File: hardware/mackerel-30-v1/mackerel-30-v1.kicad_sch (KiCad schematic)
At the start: 0 parts

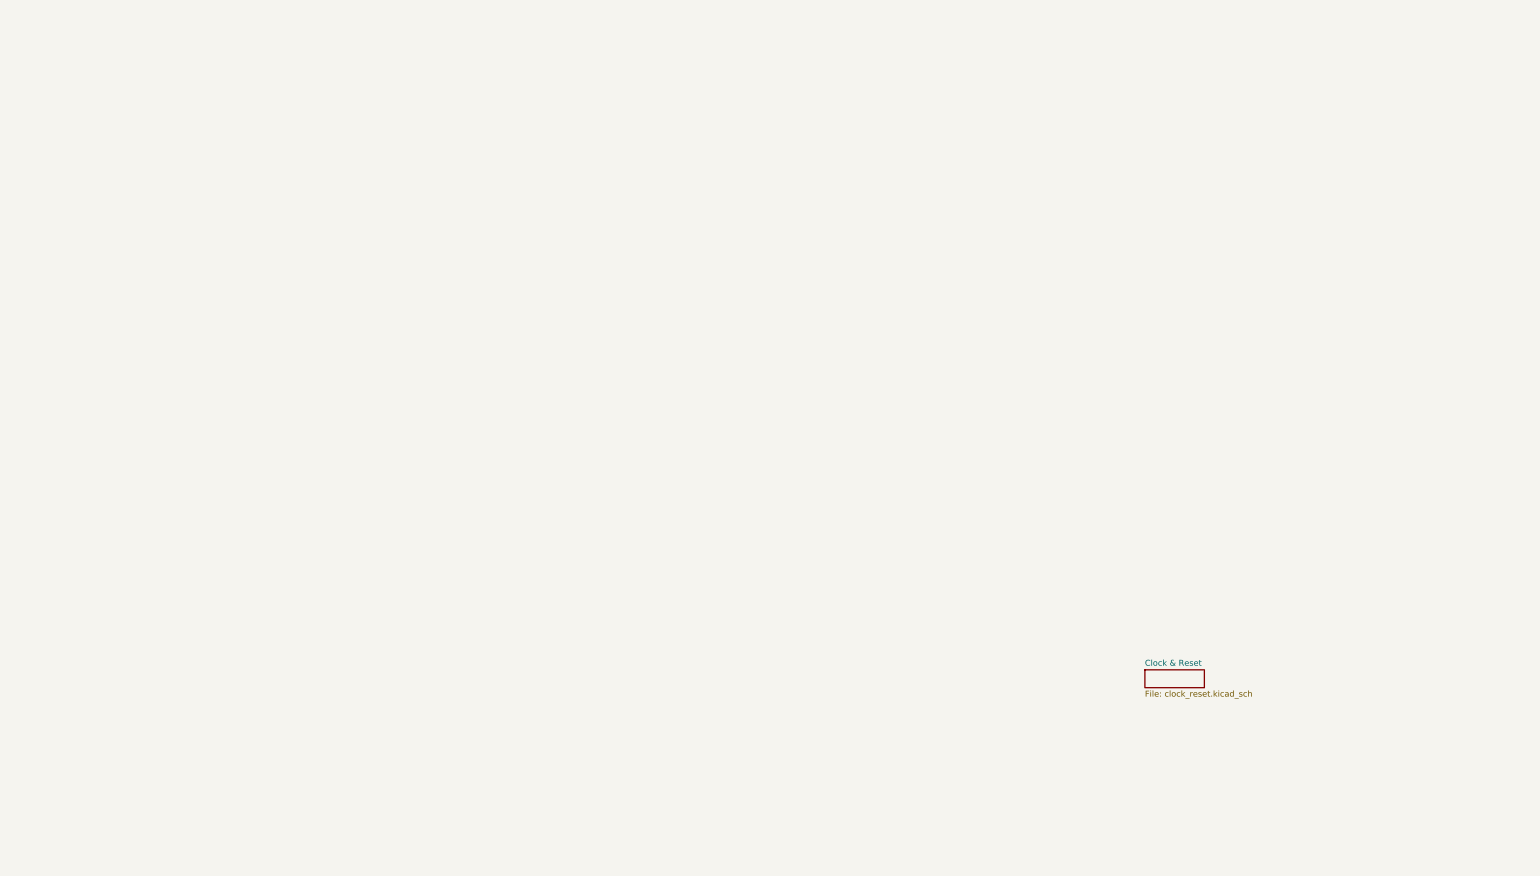
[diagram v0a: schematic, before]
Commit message: Mackerel-30: Label the 68030 pinout
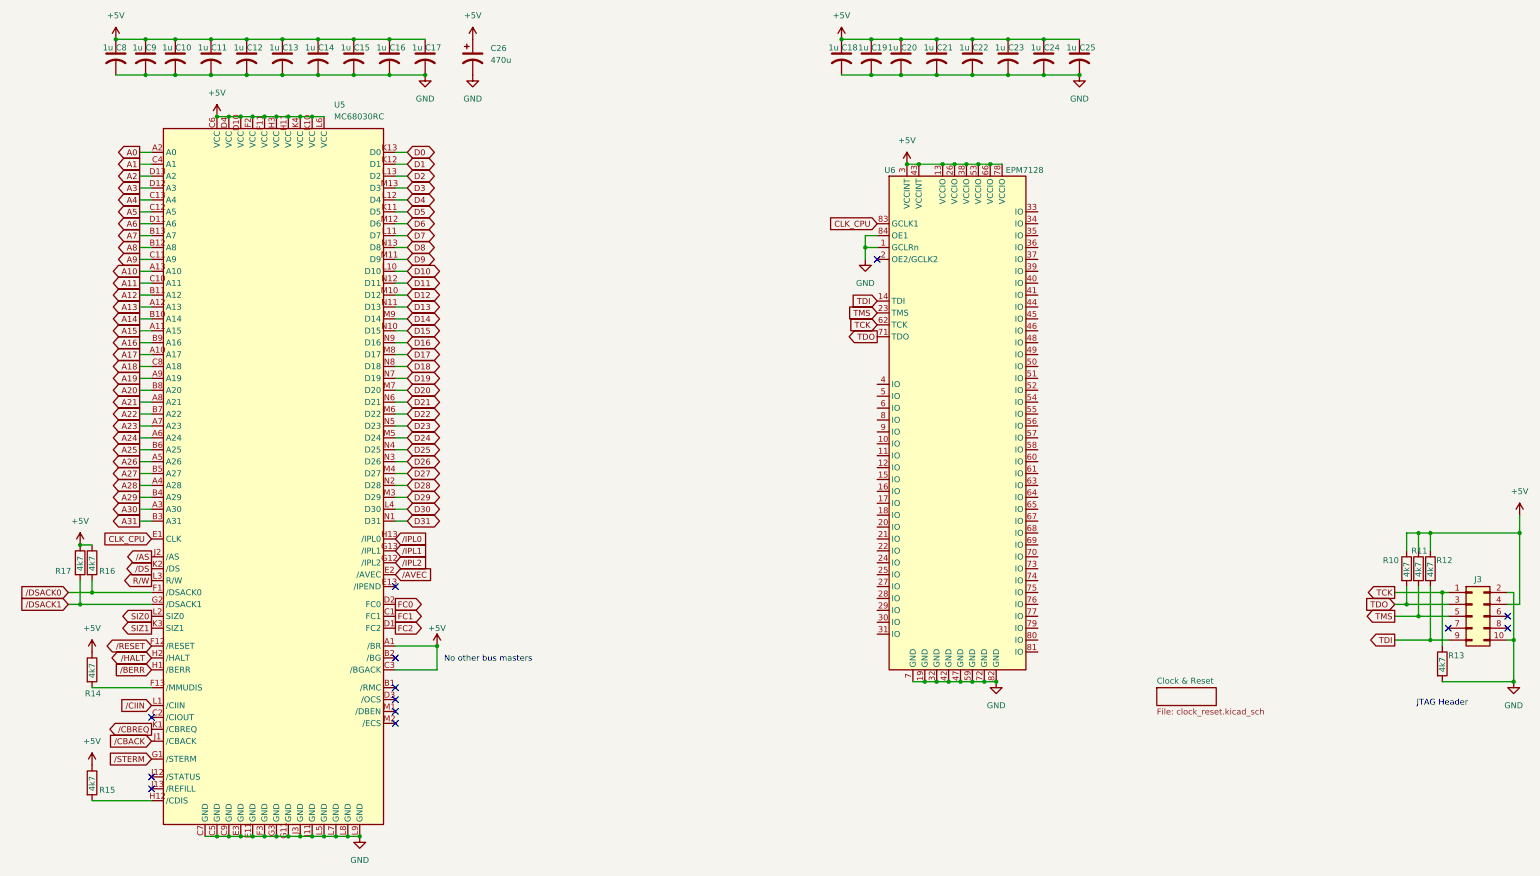
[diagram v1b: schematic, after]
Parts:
- added C10, C11, C12, C13, C14, C15, C16, C17, C18, C19, C20, C21, C22, C23, C24, C25, C8, C9: 1u, Capacitor_SMD:C_0805_2012Metric_Pad1.18x1.45mm_HandSolder, symbol Device:C_US
- added C26: 470u, Capacitor_THT:CP_Radial_D8.0mm_P3.50mm, symbol Device:C_Polarized_US
- added J3: Conn_02x05_Odd_Even, Connector_IDC:IDC-Header_2x05_P2.54mm_Vertical, symbol Connector_Generic:Conn_02x05_Odd_Even
- added R10, R11, R12, R13, R14, R15, R16, R17: 4k7, Resistor_SMD:R_0805_2012Metric_Pad1.20x1.40mm_HandSolder, symbol Device:R
- added U5: MC68030RC, mackerel:PGA169, symbol mackerel-68k-symbols:MC68030
- added U6: EPM7128, Package_LCC:PLCC-84_THT-Socket, symbol mackerel-68k-symbols:EPM7128SLC
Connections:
- new net: R14.2, U5.F13 (/MMUDIS)
- new net: R15.2, U5.H12 (/CDIS)
- new net +5V: C10.1, C11.1, C12.1, C13.1, C14.1, C15.1, C16.1, C17.1, C18.1, C19.1, C20.1, C21.1, C22.1, C23.1, C24.1, C25.1, C26.1, C8.1, C9.1, J3.4 (Pin_4), R10.1, R11.1, R12.1, R14.1, R15.1, R16.1, R17.1, U5.A1 (/BR), U5.C3 (/BGACK), U5.C6 (VCC), U5.D10 (VCC), U5.D4 (VCC), U5.F11 (VCC), U5.F2 (VCC), U5.H11 (VCC), U5.H3 (VCC), U5.K10 (VCC), U5.K4 (VCC), U5.L6 (VCC), U6.13 (VCCIO), U6.26 (VCCIO), U6.3 (VCCINT), U6.38 (VCCIO), U6.43 (VCCINT), U6.53 (VCCIO), U6.66 (VCCIO), U6.78 (VCCIO)
- new net A0: U5.A2 (A0)
- new net A1: U5.C4 (A1)
- new net A10: U5.A13 (A10)
- new net A11: U5.C10 (A11)
- new net A12: U5.B11 (A12)
- new net A13: U5.A12 (A13)
- new net A14: U5.B10 (A14)
- new net A15: U5.A11 (A15)
- new net A16: U5.B9 (A16)
- new net A17: U5.A10 (A17)
- new net A18: U5.C8 (A18)
- new net A19: U5.A9 (A19)
- new net A2: U5.D13 (A2)
- new net A20: U5.B8 (A20)
- new net A21: U5.A8 (A21)
- new net A22: U5.B7 (A22)
- new net A23: U5.A7 (A23)
- new net A24: U5.A6 (A24)
- new net A25: U5.B6 (A25)
- new net A26: U5.A5 (A26)
- new net A27: U5.B5 (A27)
- new net A28: U5.A4 (A28)
- new net A29: U5.B4 (A29)
- new net A3: U5.D12 (A3)
- new net A30: U5.A3 (A30)
- new net A31: U5.B3 (A31)
- new net A4: U5.C13 (A4)
- new net A5: U5.C12 (A5)
- new net A6: U5.D11 (A6)
- new net A7: U5.B13 (A7)
- new net A8: U5.B12 (A8)
- new net A9: U5.C11 (A9)
- new net CLK_CPU: U5.E1 (CLK), U6.83 (GCLK1)
- new net D0: U5.K13 (D0)
- new net D1: U5.K12 (D1)
- new net D10: U5.L10 (D10)
- new net D11: U5.N12 (D11)
- new net D12: U5.M10 (D12)
- new net D13: U5.N11 (D13)
- new net D14: U5.M9 (D14)
- new net D15: U5.N10 (D15)
- new net D16: U5.N9 (D16)
- new net D17: U5.M8 (D17)
- new net D18: U5.N8 (D18)
- new net D19: U5.N7 (D19)
- new net D2: U5.L13 (D2)
- new net D20: U5.M7 (D20)
- new net D21: U5.N6 (D21)
- new net D22: U5.M6 (D22)
- new net D23: U5.N5 (D23)
- new net D24: U5.M5 (D24)
- new net D25: U5.N4 (D25)
- new net D26: U5.N3 (D26)
- new net D27: U5.M4 (D27)
- new net D28: U5.N2 (D28)
- new net D29: U5.M3 (D29)
- new net D3: U5.M13 (D3)
- new net D30: U5.L4 (D30)
- new net D31: U5.N1 (D31)
- new net D4: U5.L12 (D4)
- new net D5: U5.K11 (D5)
- new net D6: U5.M12 (D6)
- new net D7: U5.L11 (D7)
- new net D8: U5.N13 (D8)
- new net D9: U5.M11 (D9)
- new net FC0: U5.D2 (FC0)
- new net FC1: U5.C1 (FC1)
- new net FC2: U5.D1 (FC2)
- new net GND: C10.2, C11.2, C12.2, C13.2, C14.2, C15.2, C16.2, C17.2, C18.2, C19.2, C20.2, C21.2, C22.2, C23.2, C24.2, C25.2, C26.2, C8.2, C9.2, J3.10 (Pin_10), J3.2 (Pin_2), R13.2, U5.C5 (GND), U5.C7 (GND), U5.C9 (GND), U5.E11 (GND), U5.E3 (GND), U5.F3 (GND), U5.G11 (GND), U5.G3 (GND), U5.J11 (GND), U5.J3 (GND), U5.L5 (GND), U5.L7 (GND), U5.L8 (GND), U5.L9 (GND), U6.1 (GCLRn), U6.19 (GND), U6.32 (GND), U6.42 (GND), U6.47 (GND), U6.59 (GND), U6.7 (GND), U6.72 (GND), U6.82 (GND), U6.84 (OE1)
- new net R/W: U5.L3 (R/W)
- new net SIZ0: U5.L2 (SIZ0)
- new net SIZ1: U5.K3 (SIZ1)
- new net TCK: J3.1 (Pin_1), R13.1, U6.62 (TCK)
- new net TDI: J3.9 (Pin_9), R12.2, U6.14 (TDI)
- new net TDO: J3.3 (Pin_3), R10.2, U6.71 (TDO)
- new net TMS: J3.5 (Pin_5), R11.2, U6.23 (TMS)
- new net /AS: U5.J2 (/AS)
- new net /AVEC: U5.E2 (/AVEC)
- new net /BERR: U5.H1 (/BERR)
- new net /CBACK: U5.J1 (/CBACK)
- new net /CBREQ: U5.K1 (/CBREQ)
- new net /CIIN: U5.L1 (/CIIN)
- new net /DS: U5.K2 (/DS)
- new net /DSACK0: R16.2, U5.F1 (/DSACK0)
- new net /DSACK1: R17.2, U5.G2 (/DSACK1)
- new net /HALT: U5.H2 (/HALT)
- new net /IPL0: U5.H13 (/IPL0)
- new net /IPL1: U5.G13 (/IPL1)
- new net /IPL2: U5.G12 (/IPL2)
- new net /RESET: U5.F12 (/RESET)
- new net /STERM: U5.G1 (/STERM)
- no-connect marks 0 -> 13
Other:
- note added: "JTAG Header"
- note added: "No other bus masters"

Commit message: Mackerel-30: Add low mem, FPU, DRAM, DUART, IDE, power sheets to schematic
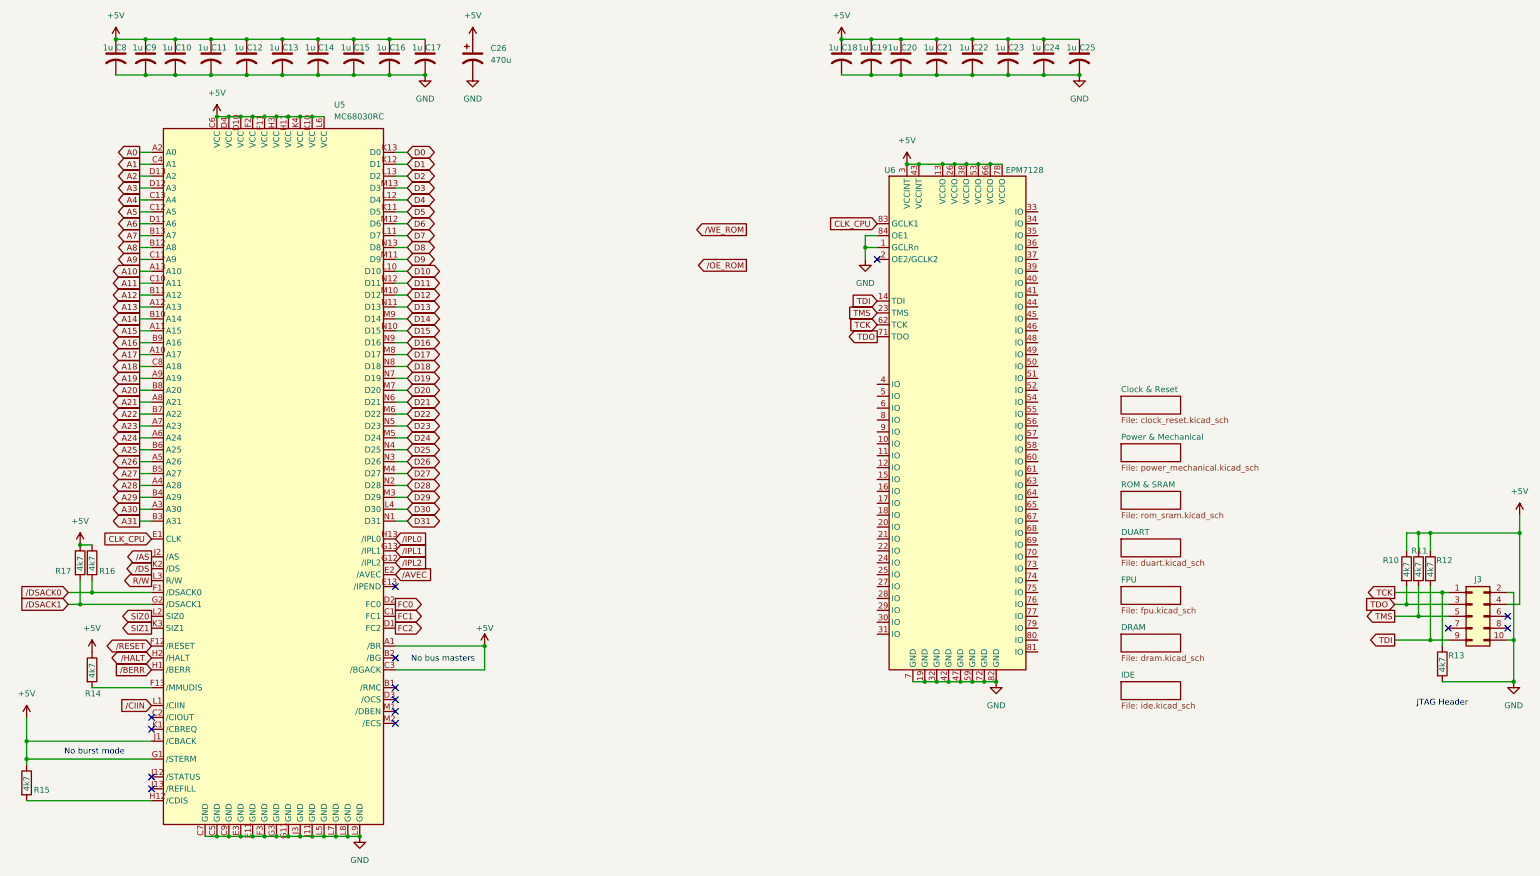
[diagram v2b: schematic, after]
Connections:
- net /CBACK is gone; now on net +5V: U5.J1 (/CBACK)
- net /STERM is gone; now on net +5V: U5.G1 (/STERM)
- net /CBREQ: no longer names the net of U5.K1 (/CBREQ)
- no-connect marks 13 -> 14
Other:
- added sheet DRAM (dram.kicad_sch)
- added sheet DUART (duart.kicad_sch)
- added sheet FPU (fpu.kicad_sch)
- added sheet IDE (ide.kicad_sch)
- added sheet Power & Mechanical (power_mechanical.kicad_sch)
- added sheet ROM & SRAM (rom_sram.kicad_sch)
- note added: "No burst mode"
- note added: "No bus masters"
- note removed: "No other bus masters"
- moved on the sheet: R15

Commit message: SIMM and data buffers mostly routed
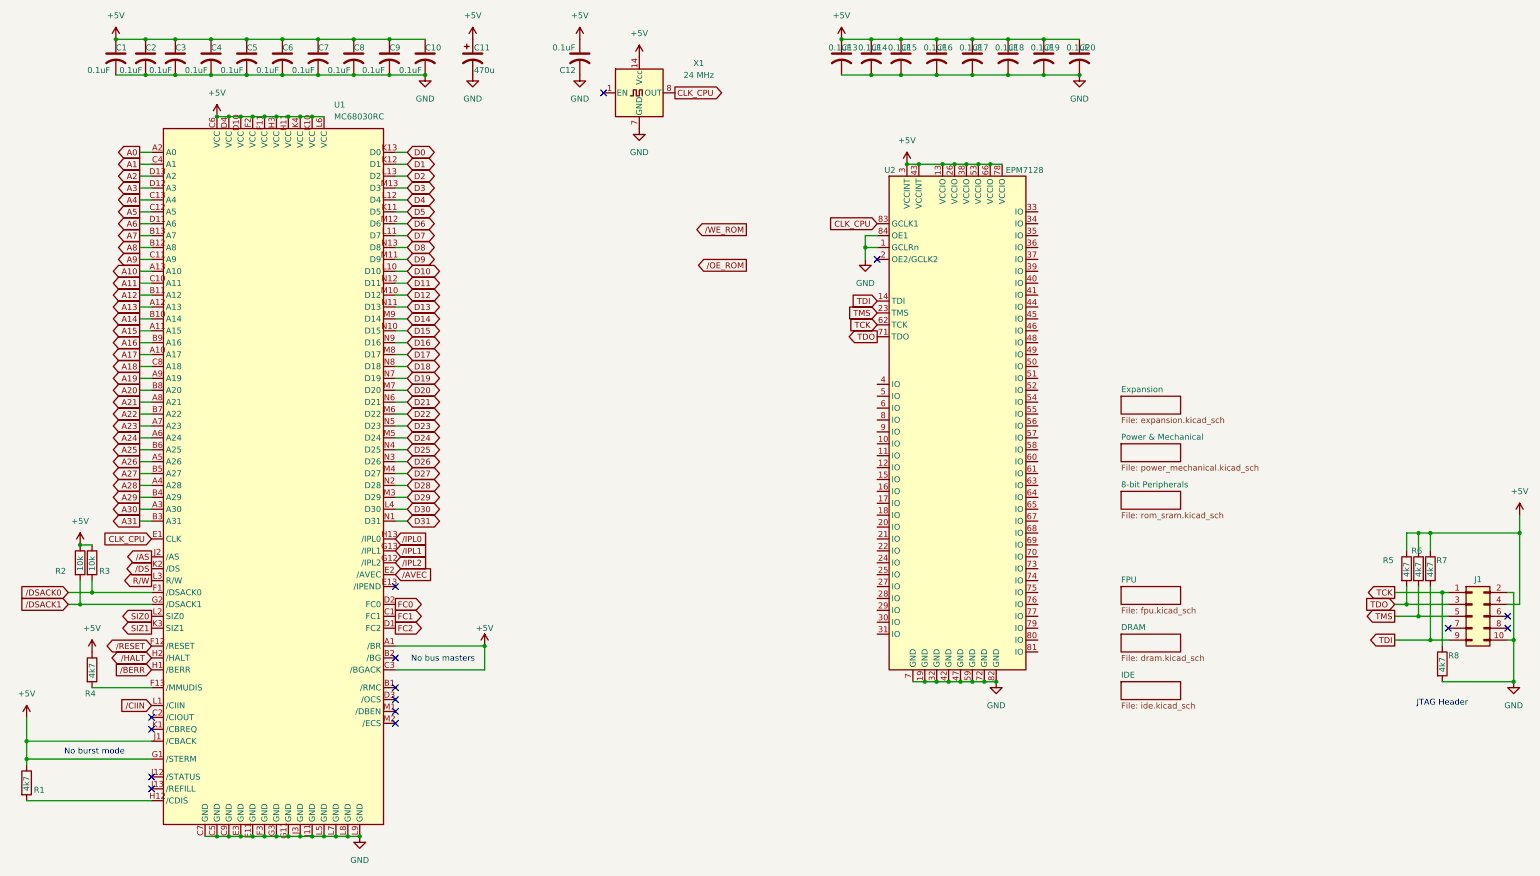
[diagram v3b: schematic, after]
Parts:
- added C12: 0.1uF, Capacitor_SMD:C_1206_3216Metric_Pad1.33x1.80mm_HandSolder, symbol Device:C_US
- added X1: 24 MHz, Oscillator:Oscillator_DIP-14, symbol Oscillator:CXO_DIP14
- C1: renamed from C8; value 1u -> 0.1uF; footprint Capacitor_SMD:C_0805_2012Metric_Pad1.18x1.45mm_HandSolder -> Capacitor_SMD:C_1206_3216Metric_Pad1.33x1.80mm_HandSolder
- C10: renamed from C17; value 1u -> 0.1uF; footprint Capacitor_SMD:C_0805_2012Metric_Pad1.18x1.45mm_HandSolder -> Capacitor_SMD:C_1206_3216Metric_Pad1.33x1.80mm_HandSolder
- C13: renamed from C18; value 1u -> 0.1uF; footprint Capacitor_SMD:C_0805_2012Metric_Pad1.18x1.45mm_HandSolder -> Capacitor_SMD:C_1206_3216Metric_Pad1.33x1.80mm_HandSolder
- C14: renamed from C19; value 1u -> 0.1uF; footprint Capacitor_SMD:C_0805_2012Metric_Pad1.18x1.45mm_HandSolder -> Capacitor_SMD:C_1206_3216Metric_Pad1.33x1.80mm_HandSolder
- C15: renamed from C20; value 1u -> 0.1uF; footprint Capacitor_SMD:C_0805_2012Metric_Pad1.18x1.45mm_HandSolder -> Capacitor_SMD:C_1206_3216Metric_Pad1.33x1.80mm_HandSolder
- C16: renamed from C21; value 1u -> 0.1uF; footprint Capacitor_SMD:C_0805_2012Metric_Pad1.18x1.45mm_HandSolder -> Capacitor_SMD:C_1206_3216Metric_Pad1.33x1.80mm_HandSolder
- C17: renamed from C22; value 1u -> 0.1uF; footprint Capacitor_SMD:C_0805_2012Metric_Pad1.18x1.45mm_HandSolder -> Capacitor_SMD:C_1206_3216Metric_Pad1.33x1.80mm_HandSolder
- C18: renamed from C23; value 1u -> 0.1uF; footprint Capacitor_SMD:C_0805_2012Metric_Pad1.18x1.45mm_HandSolder -> Capacitor_SMD:C_1206_3216Metric_Pad1.33x1.80mm_HandSolder
- C19: renamed from C24; value 1u -> 0.1uF; footprint Capacitor_SMD:C_0805_2012Metric_Pad1.18x1.45mm_HandSolder -> Capacitor_SMD:C_1206_3216Metric_Pad1.33x1.80mm_HandSolder
- C2: renamed from C9; value 1u -> 0.1uF; footprint Capacitor_SMD:C_0805_2012Metric_Pad1.18x1.45mm_HandSolder -> Capacitor_SMD:C_1206_3216Metric_Pad1.33x1.80mm_HandSolder
- C20: renamed from C25; value 1u -> 0.1uF; footprint Capacitor_SMD:C_0805_2012Metric_Pad1.18x1.45mm_HandSolder -> Capacitor_SMD:C_1206_3216Metric_Pad1.33x1.80mm_HandSolder
- C3: renamed from C10; value 1u -> 0.1uF; footprint Capacitor_SMD:C_0805_2012Metric_Pad1.18x1.45mm_HandSolder -> Capacitor_SMD:C_1206_3216Metric_Pad1.33x1.80mm_HandSolder
- C4: renamed from C11; value 1u -> 0.1uF; footprint Capacitor_SMD:C_0805_2012Metric_Pad1.18x1.45mm_HandSolder -> Capacitor_SMD:C_1206_3216Metric_Pad1.33x1.80mm_HandSolder
- C5: renamed from C12; value 1u -> 0.1uF; footprint Capacitor_SMD:C_0805_2012Metric_Pad1.18x1.45mm_HandSolder -> Capacitor_SMD:C_1206_3216Metric_Pad1.33x1.80mm_HandSolder
- C6: renamed from C13; value 1u -> 0.1uF; footprint Capacitor_SMD:C_0805_2012Metric_Pad1.18x1.45mm_HandSolder -> Capacitor_SMD:C_1206_3216Metric_Pad1.33x1.80mm_HandSolder
- C7: renamed from C14; value 1u -> 0.1uF; footprint Capacitor_SMD:C_0805_2012Metric_Pad1.18x1.45mm_HandSolder -> Capacitor_SMD:C_1206_3216Metric_Pad1.33x1.80mm_HandSolder
- C8: renamed from C15; value 1u -> 0.1uF; footprint Capacitor_SMD:C_0805_2012Metric_Pad1.18x1.45mm_HandSolder -> Capacitor_SMD:C_1206_3216Metric_Pad1.33x1.80mm_HandSolder
- C9: renamed from C16; value 1u -> 0.1uF; footprint Capacitor_SMD:C_0805_2012Metric_Pad1.18x1.45mm_HandSolder -> Capacitor_SMD:C_1206_3216Metric_Pad1.33x1.80mm_HandSolder
- R1: renamed from R15; footprint Resistor_SMD:R_0805_2012Metric_Pad1.20x1.40mm_HandSolder -> Resistor_SMD:R_1206_3216Metric_Pad1.30x1.75mm_HandSolder
- R2: renamed from R17; value 4k7 -> 10k; footprint Resistor_SMD:R_0805_2012Metric_Pad1.20x1.40mm_HandSolder -> Resistor_SMD:R_1206_3216Metric_Pad1.30x1.75mm_HandSolder
- R3: renamed from R16; value 4k7 -> 10k; footprint Resistor_SMD:R_0805_2012Metric_Pad1.20x1.40mm_HandSolder -> Resistor_SMD:R_1206_3216Metric_Pad1.30x1.75mm_HandSolder
- R4: renamed from R14; footprint Resistor_SMD:R_0805_2012Metric_Pad1.20x1.40mm_HandSolder -> Resistor_SMD:R_1206_3216Metric_Pad1.30x1.75mm_HandSolder
- R5: renamed from R10; footprint Resistor_SMD:R_0805_2012Metric_Pad1.20x1.40mm_HandSolder -> Resistor_SMD:R_1206_3216Metric_Pad1.30x1.75mm_HandSolder
- R6: renamed from R11; footprint Resistor_SMD:R_0805_2012Metric_Pad1.20x1.40mm_HandSolder -> Resistor_SMD:R_1206_3216Metric_Pad1.30x1.75mm_HandSolder
- R7: renamed from R12; footprint Resistor_SMD:R_0805_2012Metric_Pad1.20x1.40mm_HandSolder -> Resistor_SMD:R_1206_3216Metric_Pad1.30x1.75mm_HandSolder
- R8: renamed from R13; footprint Resistor_SMD:R_0805_2012Metric_Pad1.20x1.40mm_HandSolder -> Resistor_SMD:R_1206_3216Metric_Pad1.30x1.75mm_HandSolder
- renumbered C26 to C11, J3 to J1, U5 to U1, U6 to U2
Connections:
- net +5V: now also C12.1, X1.14 (Vcc)
- net CLK_CPU: now also X1.8 (OUT)
- net GND: now also C12.2, X1.7 (GND)
- no-connect marks 14 -> 15
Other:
- sheet ROM & SRAM renamed 8-bit Peripherals
- removed sheet Clock & Reset
- removed sheet DUART
- added sheet Expansion (expansion.kicad_sch)
